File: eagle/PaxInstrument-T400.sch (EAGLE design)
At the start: 136 parts, among them IC1 MCP3424, IC3 SN74LVC1G74DCT, J1 MICRO-SDCARD-CONNECTOR-330006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, Q1 DMP2035U-7, Q2 DMP2035U-7, Q3 DMN2075U-7, Q4 DMN2075U-7, Q5 DMP2035U-7, U1 MCP9800, U2 APX809, U3 MCP73831, U4 MIC5219-3.3V, X1 FH12-12S-1S, Y1 RESONATORSMD

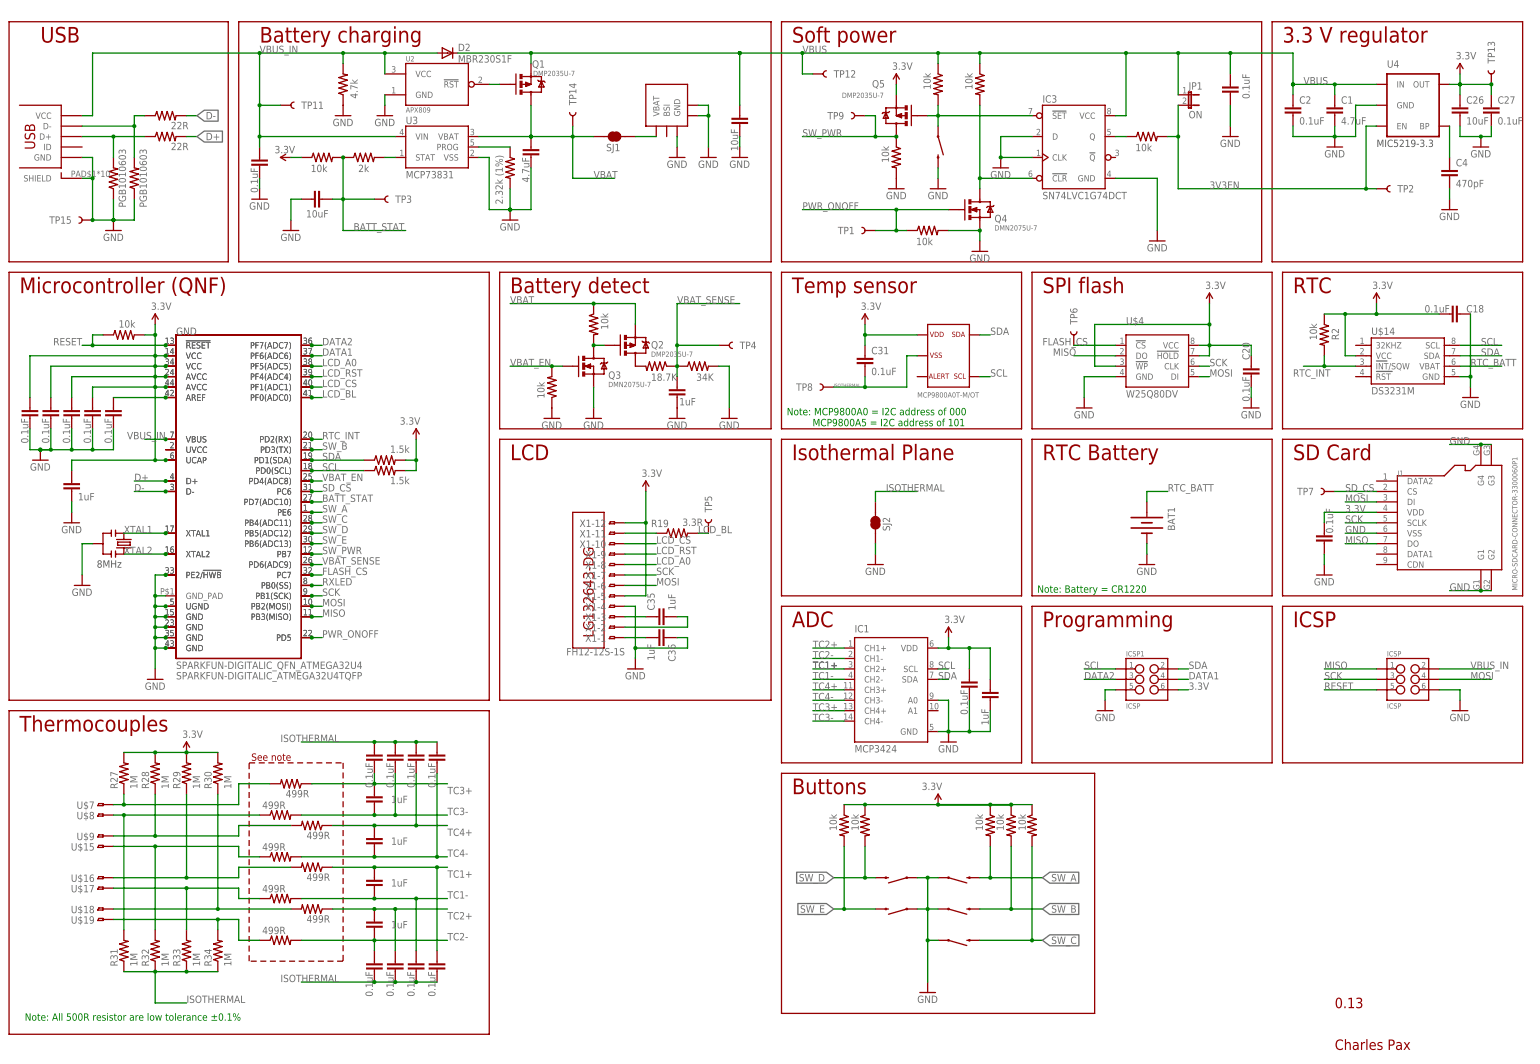
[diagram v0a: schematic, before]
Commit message: Remove a lot and replace atmega with stm32f103
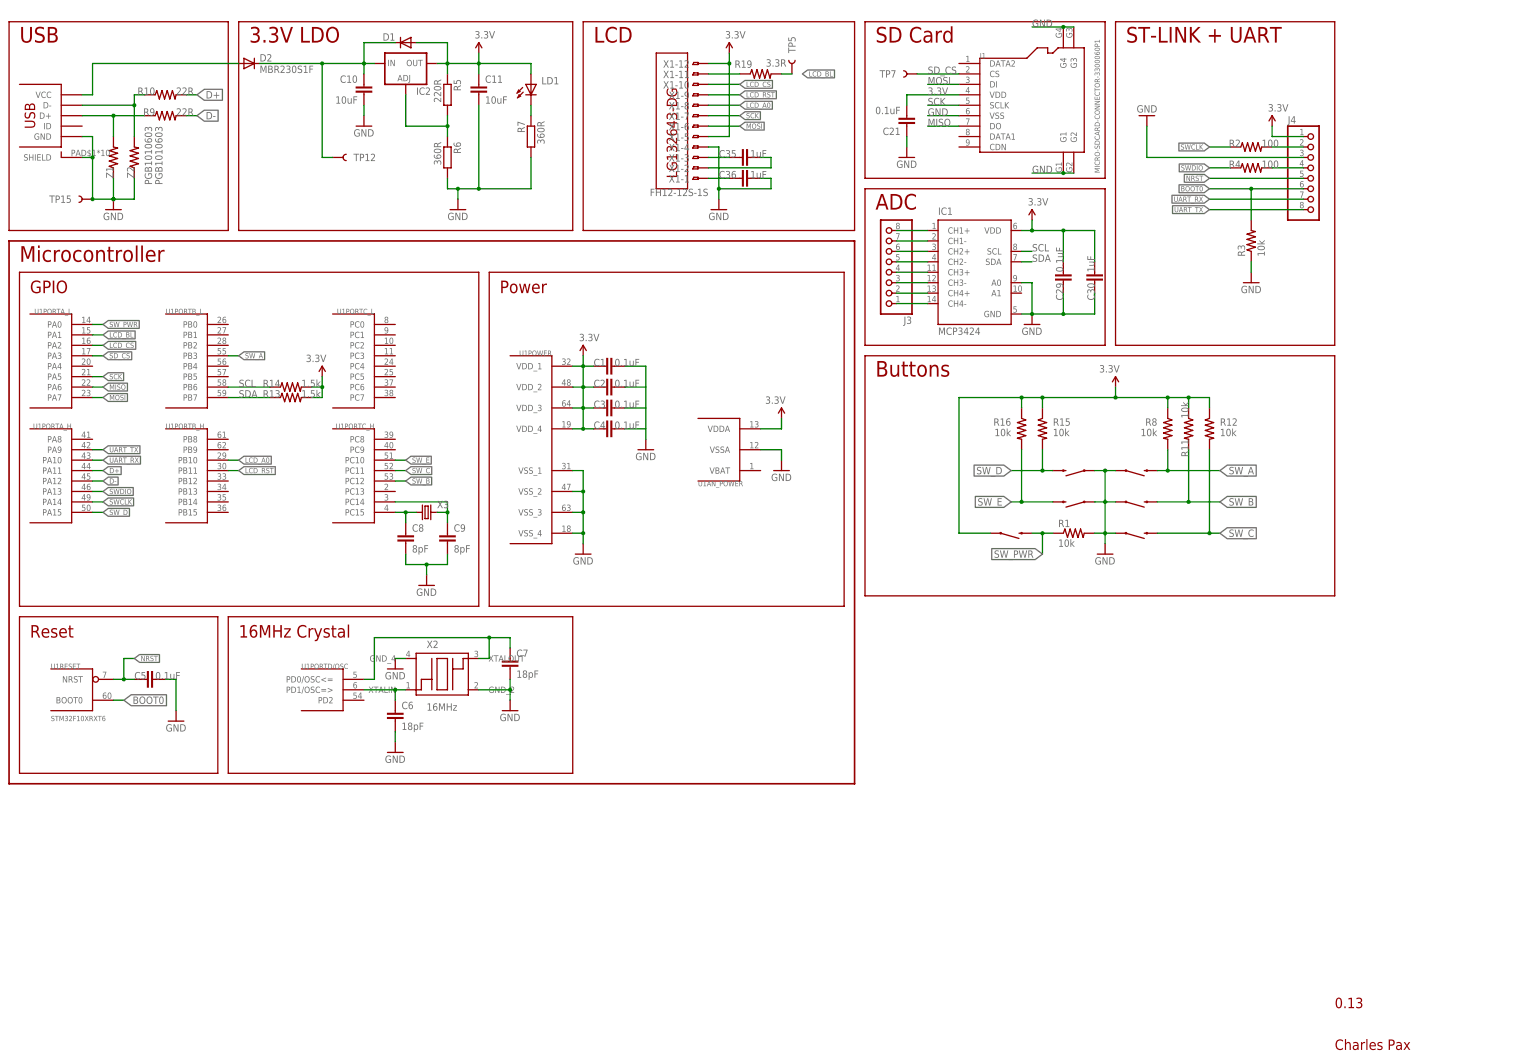
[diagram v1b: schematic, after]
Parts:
- removed BAT1: (no value), SparkFun-Electromechanical:BATTERY12MM
- removed C12, C22, C26: 10uF, PaxInstrument-T400:SPARKFUN-CAPACITORS_CAP0603-CAP
- removed C13, C14, C15, C16, C17, C18, C20, C24, C25, C27, C28, C31, C32, C33, C34, C37: 0.1uF, PaxInstrument-T400:SPARKFUN-CAPACITORS_CAP0603-CAP
- removed C19, C23: 1uF, PaxInstrument-T400:SPARKFUN-CAPACITORS_CAP0603-CAP
- removed GND: SPARKFUN-DIGITALIC_QFN_ATMEGA32U4, PaxInstrument-T400:SPARKFUN-DIGITALIC_QFN_ATMEGA32U4
- removed IC3: SN74LVC1G74DCT, PaxInstrument-T400:SN74LVC1G74DCT
- removed ICSP, ICSP1: ICSP, PaxInstrument-T400:SPARKFUN-CONNECTORS_M03X2PAX
- removed JP1: ON, SparkFun-Passives:JUMPER-2SMD-NO
- removed Q1, Q2, Q5: DMP2035U-7, PaxInstrument-T400:MOSFET-PCHANNELSMT
- removed Q3, Q4: DMN2075U-7, PaxInstrument-T400:MOSFET-NCHANNELSMT
- removed R17: 2k, PaxInstrument-T400:SPARKFUN-RESISTORS_RESISTOR0603-RES
- removed R18, R21, R22, R23: 10k, PaxInstrument-T400:SPARKFUN-RESISTORS_RESISTOR0603-RES
- removed R20: 18.7K, PaxInstrument-T400:SPARKFUN-RESISTORS_RESISTOR0603-RES
- removed R24: 34K, PaxInstrument-T400:SPARKFUN-RESISTORS_RESISTOR0603-RES
- removed R25: 4.7k, PaxInstrument-T400:SPARKFUN-RESISTORS_RESISTOR0603-RES
- removed R27, R28, R29, R30, R31, R32, R33, R34: 1M, PaxInstrument-T400:SPARKFUN-RESISTORS_RESISTOR0603-RES
- removed R35, R36, R37, R38, R39, R40, R41, R42: 499R, PaxInstrument-T400:SPARKFUN-RESISTORS_RESISTOR0603-RES
- removed SJ1, SJ2: JUMPER-PAD-2-NC_BY_TRACE, SparkFun-Passives:JUMPER-PAD-2-NC_BY_TRACE
- removed TP1: PWR_ONOFF, PaxInstrument-T400:TEST-POINTTP_15TH_THRU
- removed TP11: VBUS_IN, PaxInstrument-T400:TEST-POINTTP_15TH_THRU
- removed TP13: 3.3V, PaxInstrument-T400:TEST-POINTTP_15TH_THRU
- removed TP14: VBAT, PaxInstrument-T400:TEST-POINTTP_15TH_THRU
- removed TP2: 3V3_EN, PaxInstrument-T400:TEST-POINTTP_15TH_THRU
- removed TP3: BATT_STAT, PaxInstrument-T400:TEST-POINTTP_15TH_THRU
- removed TP4: VBAT_SENSE, PaxInstrument-T400:TEST-POINTTP_15TH_THRU
- removed TP6: FLASH_CS, PaxInstrument-T400:TEST-POINTTP_15TH_THRU
- removed TP8: ISOTHERMAL, PaxInstrument-T400:TEST-POINTTP_15TH_THRU
- removed TP9: SW_PWR, PaxInstrument-T400:TEST-POINTTP_15TH_THRU
- removed U$1: USB_MICROSMT+THRUHULE, blinkinlabs:USB_MICROSMT+THRUHULE
- removed U$14: DS3231M, charlespax:DS3231M
- removed U$15, U$16, U$17, U$18, U$19, U$7, U$8, U$9: TC-MINI-SINGLE, PaxInstruments-Connectors:TC-MINI-SINGLE
- removed U$2: BL-5C-CONNECTOR, charlespax:BL-5C-CONNECTOR
- removed U$3: SPARKFUN-DIGITALIC_ATMEGA32U4TQFP, PaxInstrument-T400:SPARKFUN-DIGITALIC_ATMEGA32U4TQFP
- removed U$4: W25Q80DV, PaxInstrument-T400:W25Q80BV
- removed U2: APX809, PaxInstrument-T400:APX809
- removed U3: MCP73831, SparkFun-PowerIC:MCP73831
- removed U4: MIC5219-3.3V, SparkFun:V_REG_LDOSMD
- removed Y1: RESONATORSMD, SparkFun:RESONATORSMD
- added D1: 1N4148W, diode:CGRM4001-G
- added IC2: LM317AEMP, v-reg:LM317MSTT3
- added J2: USB_MICROSMT+THRUHULE, blinkinlabs:USB_MICROSMT+THRUHULE
- added J3, J4: (no value), pinhead:PINHD-1X8
- added LD1: (no value), adafruit:LEDCHIPLED_0805
- added X2: 16MHz, crystals:FA-238
- added X3: (no value), crystal:CRYSTALTC26H
- C1: value 4.7uF -> 0.1uF
- C10, C11: value 1uF -> 10uF; device PaxInstrument-T400:SPARKFUN-CAPACITORS_CAP0603-CAP -> ell-i:C0603
- C4: value 470pF -> 0.1uF
- C6: value 0.1uF -> 18pF
- C7: value 1uF -> 18pF
- C8: value 1uF -> 8pF
- C9: value 4.7uF -> 8pF
- R1: POPULATE (none) -> DNP
- R2, R4: value 10k -> 100; POPULATE (none) -> DNP
- R3: value 2.32k (1%) -> 10k; POPULATE (none) -> DNP
- R5: value 10k -> 220R; device PaxInstrument-T400:SPARKFUN-RESISTORS_RESISTOR0603-RES -> ell-i:R0603
- R6, R7: value 10k -> 360R; device PaxInstrument-T400:SPARKFUN-RESISTORS_RESISTOR0603-RES -> ell-i:R0603
- U1: value MCP9800 -> STM32F10XRXT6; device newparts_2010:MCP9800 -> stm32:STM32F10XRXT6; MF Microchip Technology -> (none); MPN MCP9800A0T-M/OT -> (none)
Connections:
- removed net 3V3EN: JP1.2, R21.2, TP2.1, U4.EN
- removed net BATT_STAT: C22.1, GND.PD7(ADC10), R1.2, R17.1, TP3.1, U$3.PD7(ADC10)
- removed net DATA1: GND.PF6(ADC6), ICSP1.4, U$3.PF6(ADC6)
- removed net DATA2: GND.PF7(ADC7), ICSP1.3, U$3.PF7(ADC7)
- removed net FLASH_CS: GND.PC7, TP6.1, U$3.PC7, U$4.!CS
- removed net ISOTHERMAL: C13.2, C14.2, C15.2, C16.2, C17.1, C24.1, C25.1, C31.2, C37.1, R31.1, R32.1, R33.1, R34.1, SJ2.2, TP8.1, U1.2
- removed net N$11: R27.1, R35.2, U$7.1
- removed net N$12: Q1.G, U2.!RST
- removed net N$15: C3.1, GND.AREF, U$3.AREF
- removed net N$20: Q2.D, R20.2
- removed net N$26: Q2.G, Q3.D, R5.2
- removed net N$28: IC3.Q, R21.1
- removed net N$34: R32.2, R38.1, U$15.1
- removed net N$35: R28.1, R37.2, U$9.1
- removed net N$40: R30.1, R40.2, U$18.1
- removed net PWR_ONOFF: GND.PD5, Q4.G, R22.1, TP1.1, U$3.PD5
- removed net RESET: GND.!RESET, ICSP.5, R4.1, U$3.!RESET
- removed net RTC_BATT: BAT1.+, U$14.VBAT
- removed net RTC_INT: GND.PD2(RX), R2.2, U$14.INT/SQW, U$3.PD2(RX)
- removed net RXLED: GND.PB0(SS), U$3.PB0(SS)
- removed net TC1+: C10.1, C16.1, IC1.CH2+, R39.1
- removed net TC1-: C10.2, C15.1, IC1.CH2-, R41.2
- removed net TC2+: C11.1, C14.1, IC1.CH1+, R40.1
- removed net TC2-: C11.2, C13.1, IC1.CH1-, R42.2
- removed net TC3+: C17.2, C7.1, IC1.CH4+, R35.1
- removed net TC3-: C24.2, C7.2, IC1.CH4-, R36.2
- removed net TC4+: C25.2, C8.1, IC1.CH3+, R37.1
- removed net TC4-: C37.2, C8.2, IC1.CH3-, R38.2
- removed net VBAT: C9.1, Q1.D, Q2.S, R5.1, SJ1.1, TP14.1, U3.VBAT
- removed net VBAT_EN: GND.PD4(ADC8), Q3.G, R23.2, U$3.PD4(ADC8)
- removed net VBAT_SENSE: C23.1, GND.PD6(ADC9), R20.1, R24.1, TP4.1, U$3.PD6(ADC9)
- removed net XTAL1: GND.XTAL1, U$3.XTAL1, Y1.1
- removed net XTAL2: GND.XTAL2, U$3.XTAL2, Y1.3
- new net ADC_CH1_N: IC1.CH1-, J3.7
- new net ADC_CH1_P: IC1.CH1+, J3.8
- new net ADC_CH2_N: IC1.CH2-, J3.5
- new net ADC_CH2_P: IC1.CH2+, J3.6
- new net ADC_CH3_N: IC1.CH3-, J3.3
- new net ADC_CH3_P: IC1.CH3+, J3.4
- new net ADC_CH4_N: IC1.CH4-, J3.1
- new net ADC_CH4_P: IC1.CH4+, J3.2
- new net BOOT0: J4.6, R3.2, U1RESET.BOOT0
- new net NRST: C5.1, J4.5, U1RESET.NRST
- new net SWCLK: R2.1, U1PORTA_H.PA14
- new net SWDIO: R4.1, U1PORTA_H.PA13
- new net UART_RX: J4.7, U1PORTA_H.PA10
- new net UART_TX: J4.8, U1PORTA_H.PA9
- net 3.3V: now also C1.1, C11.1, C2.1, C3.1, C4.1, D1.A, IC2.OUT, J4.1, LD1.A, R5.1, S6.1, U1AN_POWER.VDDA, U1POWER.VDD_1, U1POWER.VDD_2, U1POWER.VDD_3, U1POWER.VDD_4; no longer C18.1, C19.1, C20.2, C26.1, C27.1, C31.1, C32.1, C33.1, C34.1, C5.1, GND.AVCC@24, GND.AVCC@44, GND.UCAP, GND.VCC@14, GND.VCC@34, ICSP1.6, Q5.S, R1.1, R2.1, R27.2, R28.2, R29.2, R30.2, R4.2, TP13.1, U$14.VCC, U$3.AVCC@24, U$3.AVCC@44, U$3.UCAP, U$3.VCC@14, U$3.VCC@34, U$4.!HOLD, U$4.!WP, U$4.VCC, U1.1, U4.OUT
- net D+: now also R10.2, U1PORTA_H.PA11; no longer GND.D+, R9.2, U$3.D+
- net D-: now also R9.2, U1PORTA_H.PA12; no longer GND.D-, R10.2, U$3.D-
- net GND: now also C10.2, C11.2, C7.2, C8.2, J2.GND, J2.SHIELD, J4.3, R1.2, R3.1, R6.2, R7.2, U1AN_POWER.VSSA, U1POWER.VSS_1, U1POWER.VSS_2, U1POWER.VSS_3, U1POWER.VSS_4, X2.GND_2, X2.GND_4; no longer BAT1.-, C12.2, C18.2, C19.2, C2.2, C20.1, C22.2, C23.2, C26.2, C27.2, C28.2, C3.2, C32.2, C33.2, C34.2, C4.2, GND.GND@15, GND.GND@23, GND.GND@35, GND.GND@43, GND.GND_PAD, GND.PE2/!HWB, GND.UGND, IC3.CLK, IC3.D, IC3.GND, ICSP.6, ICSP1.5, Q3.S, Q4.S, R18.2, R22.2, R23.1, R24.2, R25.1, R3.2, S6.2, SJ2.1, U$1.GND, U$1.SHIELD, U$14.GND, U$2.GND, U$2.P$4, U$2.P$5, U$3.GND@15, U$3.GND@23, U$3.GND@35, U$3.GND@43, U$3.PE2/!HWB, U$3.UGND, U$4.GND, U2.GND, U3.VSS, U4.GND, Y1.2
- net LCD_A0: now also U1PORTB_H.PB10; no longer GND.PF5(ADC5), U$3.PF5(ADC5)
- net LCD_BL: now also U1PORTA_L.PA1; no longer GND.PF0(ADC0), U$3.PF0(ADC0)
- net LCD_CS: now also U1PORTA_L.PA2; no longer GND.PF1(ADC1), U$3.PF1(ADC1)
- net LCD_RST: now also U1PORTB_H.PB11; no longer GND.PF4(ADC4), U$3.PF4(ADC4)
- net MISO: now also U1PORTA_L.PA6; no longer GND.PB3(MISO), ICSP.1, U$3.PB3(MISO), U$4.DO
- net MOSI: now also U1PORTA_L.PA7; no longer GND.PB2(MOSI), ICSP.4, U$3.PB2(MOSI), U$4.DI
- net N$1: now also C7.1, U1PORTD/OSC.PD0/OSC<=, X2.XTALOUT; no longer C4.1, U4.BP
- net N$10: now also LD1.C, R7.1; no longer SJ1.2, U$2.VBAT
- net N$13: now also C3.2; no longer R29.1, R39.2, U$16.1
- net N$14: now also C4.2; no longer R33.2, R41.1, U$17.1
- net N$16: now also C8.1, U1PORTC_H.PC15, X3.1; no longer R34.2, R42.1, U$19.1
- net N$17: now also C9.1, U1PORTC_H.PC14, X3.2; no longer GND.UVCC, U$3.UVCC
- net N$2: now also C2.2; no longer R17.2, U3.STAT
- net N$25: now also J4.2, R2.2; no longer IC3.!SET, Q5.G, R6.2, S6.1
- net N$27: now also J4.4, R4.2; no longer IC3.!CLR, Q4.D, R7.2
- net N$31: now also J2.D-; no longer U$1.D-
- net N$33: now also J2.D+; no longer U$1.D+
- net N$5: now also C6.1, U1PORTD/OSC.PD1/OSC=>, X2.XTALIN; no longer R31.2, R36.1, U$8.1
- net N$7: now also IC2.ADJ, R5.2, R6.1; no longer R3.1, U3.PROG
- net SCK: now also U1PORTA_L.PA5; no longer GND.PB1(SCK), ICSP.3, U$3.PB1(SCK), U$4.CLK
- net SCL: now also U1PORTB_L.PB6; no longer GND.PD0(SCL), ICSP1.1, U$14.SCL, U$3.PD0(SCL), U1.4
- net SDA: now also U1PORTB_L.PB7; no longer GND.PD1(SDA), ICSP1.2, U$14.SDA, U$3.PD1(SDA), U1.5
- net SD_CS: now also U1PORTA_L.PA3; no longer GND.PC6, U$3.PC6
- net SW_A: now also U1PORTB_L.PB3; no longer GND.PE6, U$3.PE6
- net SW_B: now also U1PORTC_H.PC12; no longer GND.PD3(TX), U$3.PD3(TX)
- net SW_C: now also U1PORTC_H.PC11; no longer GND.PB4(ADC11), U$3.PB4(ADC11)
- net SW_D: now also U1PORTA_H.PA15; no longer GND.PB5(ADC12), U$3.PB5(ADC12)
- net SW_E: now also U1PORTC_H.PC10; no longer GND.PB6(ADC13), U$3.PB6(ADC13)
- net SW_PWR: now also R1.1, S6.2, U1PORTA_L.PA0; no longer GND.PB7, Q5.D, R18.1, TP9.1, U$3.PB7
- net VBUS: now also C10.1, D1.C, IC2.IN; no longer C1.1, C12.1, C2.1, C28.1, IC3.VCC, JP1.1, Q1.S, R6.1, R7.1, U4.IN
- net VBUS_IN: now also J2.VCC; no longer C6.1, GND.VBUS, ICSP.2, R25.2, TP11.1, U$1.VCC, U$3.VBUS, U2.VCC, U3.VIN
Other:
- note added: "16MHz Crystal"
- note added: "3.3V LDO"
- note added: "GPIO"
- note added: "Microcontroller"
- note added: "Power"
- note added: "Reset"
- note added: "ST-LINK + UART"
- note removed: "3.3 V regulator"
- note removed: "8MHz"
- note removed: "Battery charging"
- note removed: "Battery detect"
- note removed: "ICSP"
- note removed: "Isothermal Plane"
- note removed: "MIC5219-3.3"
- note removed: "Microcontroller (QNF)"
- note removed: "Note: All 500R resistor are low tolerance ±0.1%"
- note removed: "Note: Battery = CR1220"
- note removed: "Note: MCP9800A0 = I2C address of 000 MCP9800A5 = I2C address of 101"
- note removed: "Programming"
- note removed: "RTC"
- note removed: "RTC Battery"
- note removed: "SPI flash"
- note removed: "See note"
- note removed: "Soft power"
- note removed: "Temp sensor"
- note removed: "Thermocouples"
- moved on the sheet: C1, C2, C35, C36, C4, D2, IC1, J1, R19, R2, TP12, TP15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
